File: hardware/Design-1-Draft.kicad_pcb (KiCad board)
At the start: 2 copper layers, 2 parts

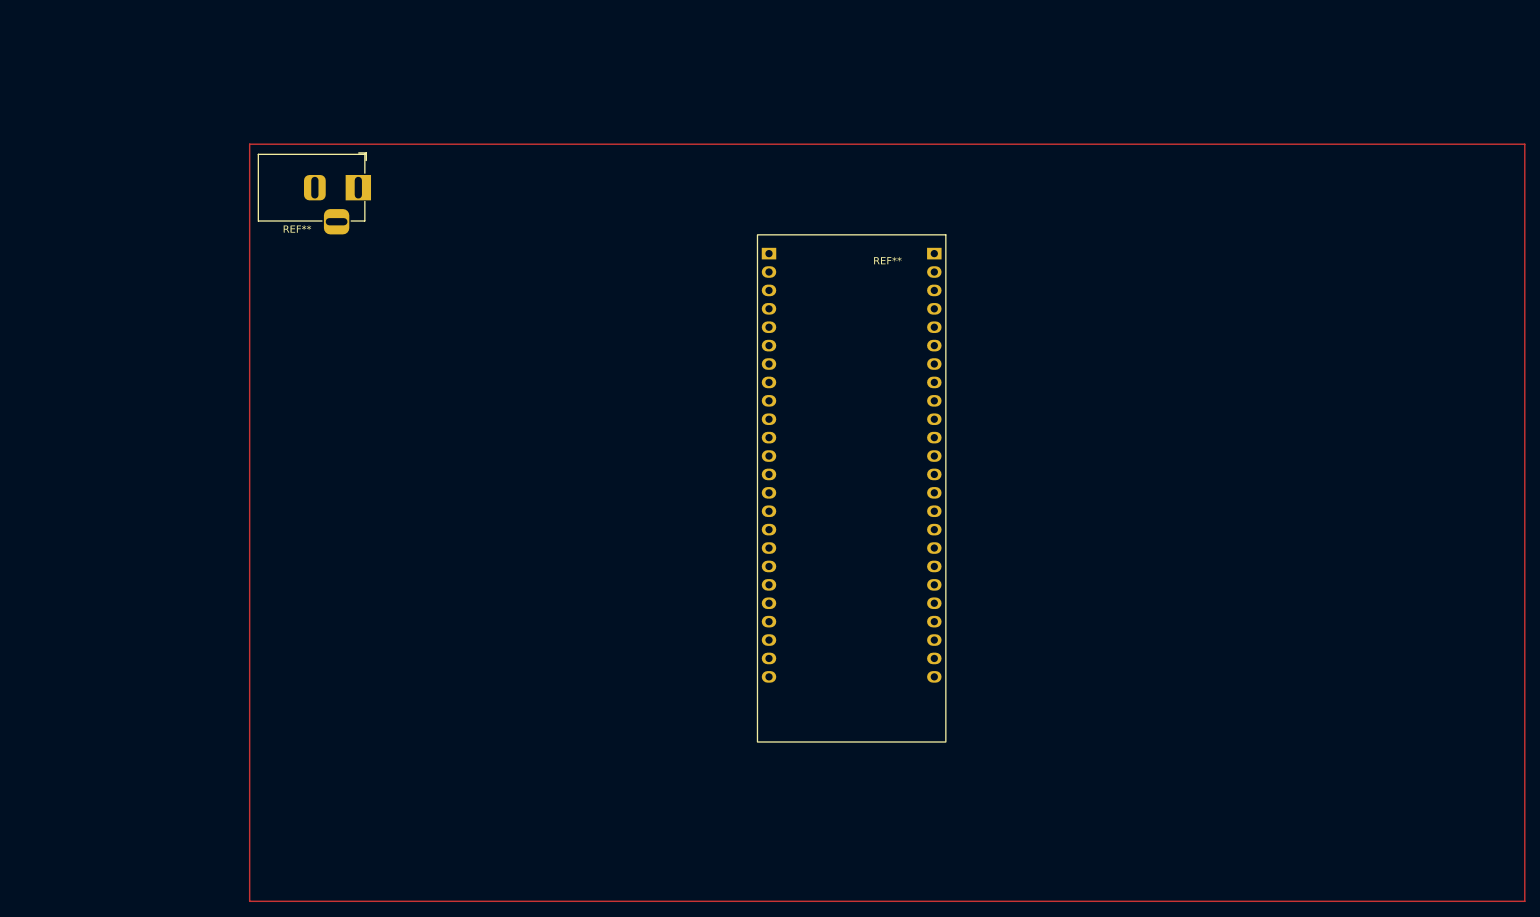
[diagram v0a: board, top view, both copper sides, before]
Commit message: added fuse, schottky, at adc sa pcb
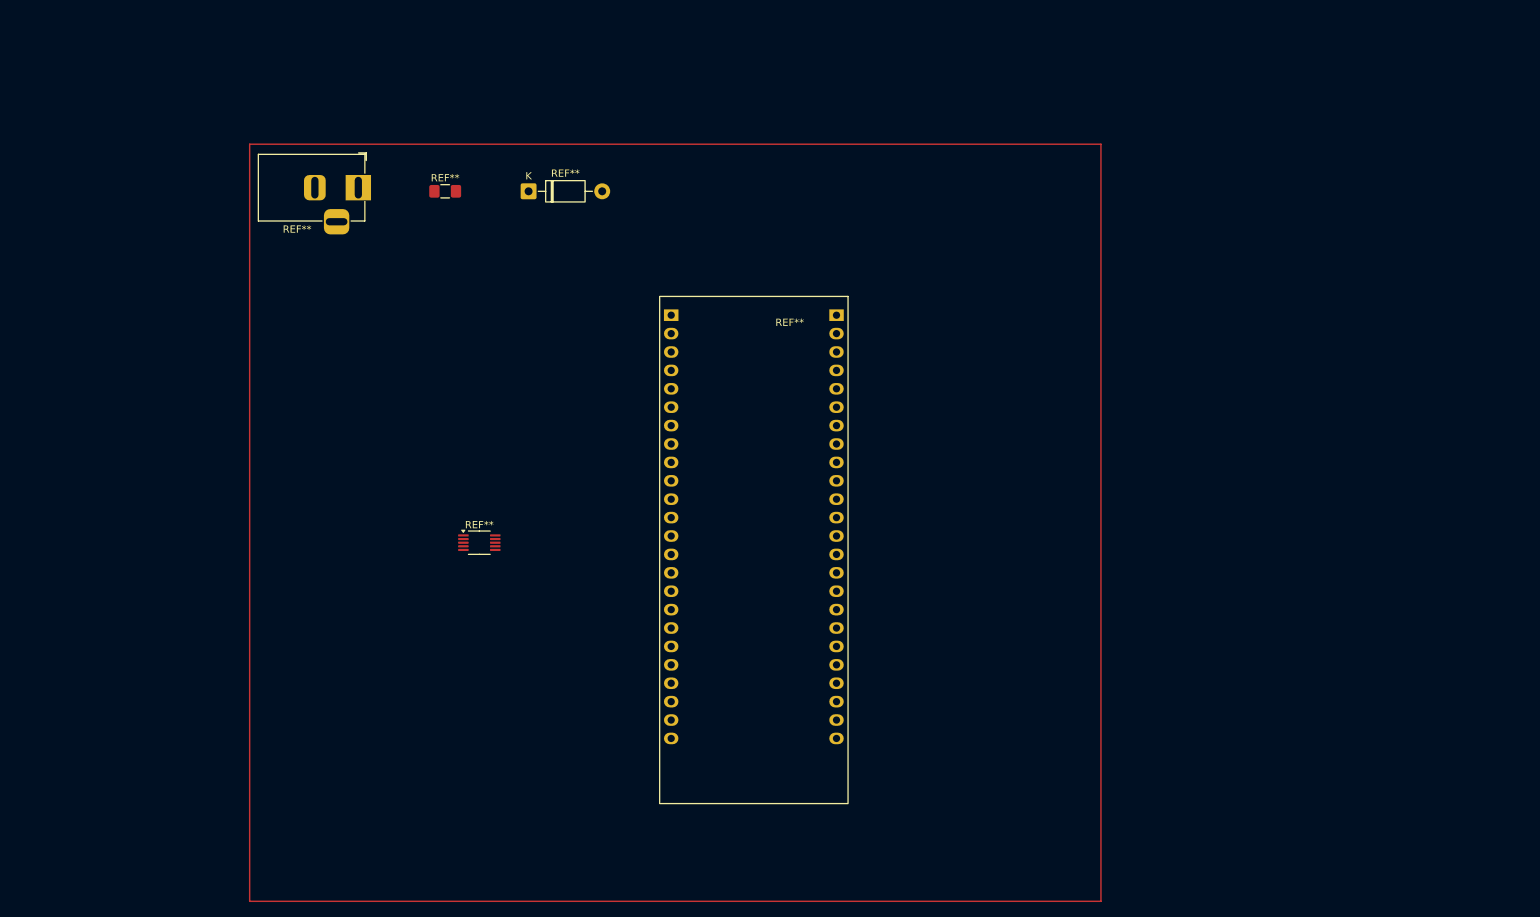
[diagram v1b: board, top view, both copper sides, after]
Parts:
- added REF**: D_DO-41_SOD81_P10.16mm_Horizontal, Diode_THT:D_DO-41_SOD81_P10.16mm_Horizontal, F.Cu at (105.0, 40.5)
- added REF**: VSSOP-10_3x3mm_P0.5mm, Package_SO:VSSOP-10_3x3mm_P0.5mm, F.Cu at (98.2, 89.0)
- added REF**: Fuse_1206_3216Metric_Pad1.42x1.75mm_HandSolder, Fuse:Fuse_1206_3216Metric_Pad1.42x1.75mm_HandSolder, F.Cu at (93.5, 40.5)
- moved REF** 16.0 mm to (136.1, 86.8)

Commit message: Assigned footprints sa schematic (kulang pa ginagawan ko pa yung iba)
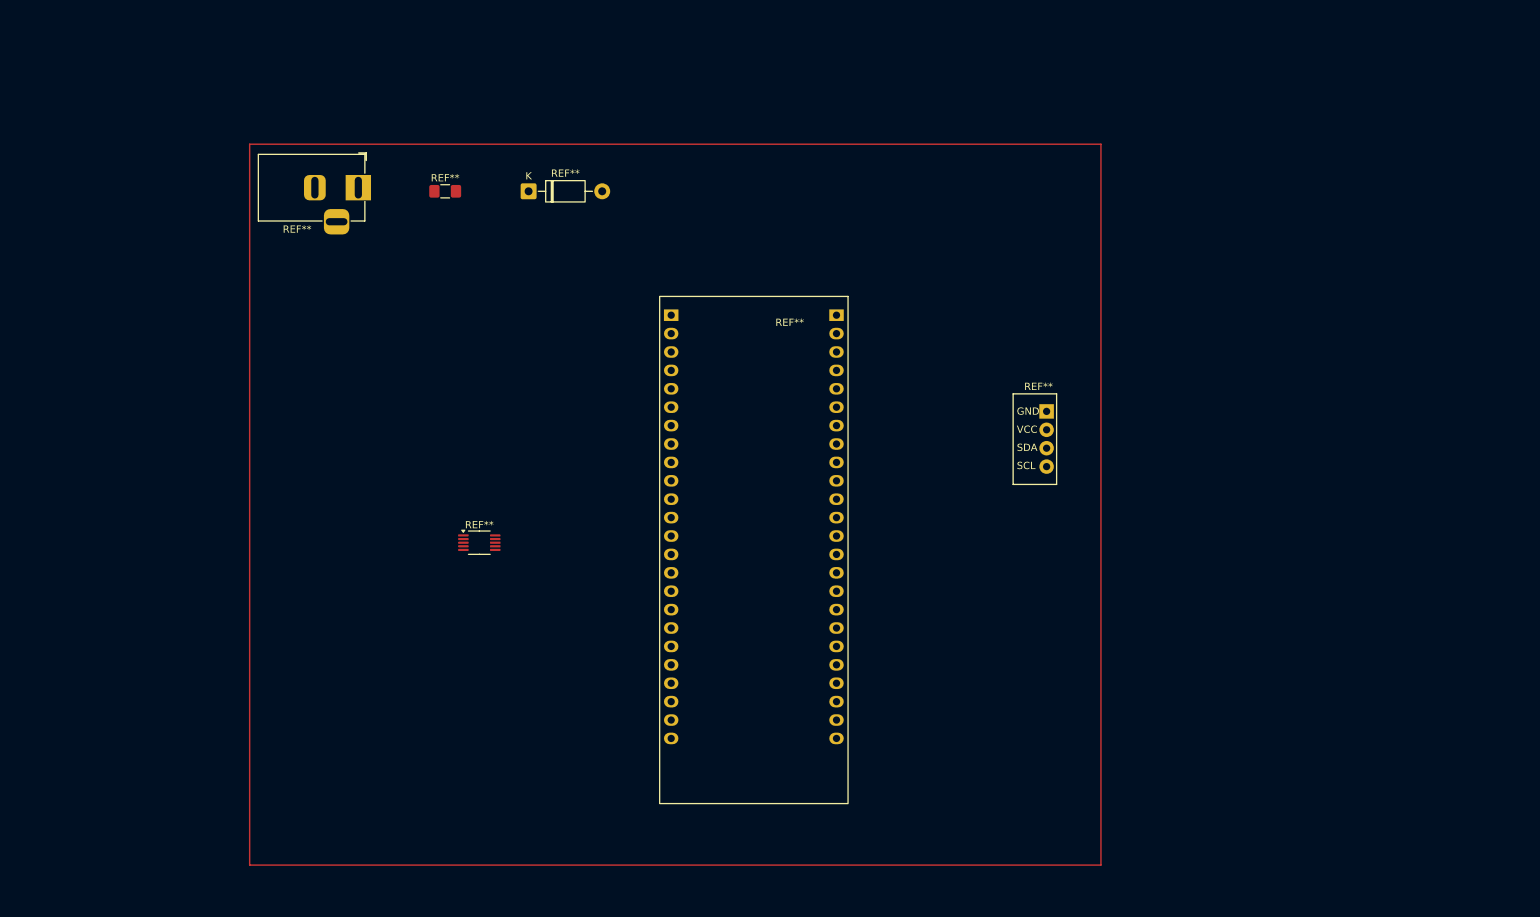
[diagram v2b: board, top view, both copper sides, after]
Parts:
- added REF**: I2C-BACKPACK-LCD, 1_CustomFootprints:I2C-BACKPACK-LCD, F.Cu at (175.0, 74.7)
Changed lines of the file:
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@@
 		)
+	)
+	(footprint "1_CustomFootprints:I2C-BACKPACK-LCD"
+		(layer "F.Cu")
+		(at 175 74.71)
+		(property "Reference" "REF**"
+			(at 0.38 -7.25 0)
+			(unlocked yes)
+			(layer "F.SilkS")
+			(effects
+				(font
+					(size 1 1)
+					(thickness 0.1)
+				)
+			)
+		)
+		(property "Value" "I2C-BACKPACK-LCD"
+			(at 0.38 7.25 0)
+			(unlocked yes)
+			(layer "F.Fab")
+			(effects
+				(font
+					(size 1 1)
+					(thickness 0.15)
+				)
+			)
+		)
+		(property "Datasheet" ""
+			(at 0 0 0)
+			(unlocked yes)
+			(layer "F.Fab")
+			(hide yes)
+			(effects
+				(font
+					(size 1 1)
+					(thickness 0.15)
+				)
+			)
+		)
+		(property "Description" ""
+			(at 0 0 0)
+			(unlocked yes)
+			(layer "F.Fab")
+			(hide yes)
+			(effects
+				(font
+					(size 1 1)
+					(thickness 0.15)
+				)
+			)
+		)
+		(attr smd)
+		(fp_line
+			(start -3.12 -6.25)
+			(end 2.88 -6.25)
+			(stroke
+				(width 0.1)
+				(type default)
+			)
+			(layer "F.SilkS")
+		)
+		(fp_line
+			(start -3.12 6.25)
+			(end -3.12 -6.25)
+			(stroke
+				(width 0.1)
+				(type default)
+			)
+			(layer "F.SilkS")
+		)
+		(fp_line
+			(start 2.88 -6.25)
+			(end 2.88 6.25)
+			(stroke
+				(width 0.1)
+				(type default)
+			)
+			(layer "F.SilkS")
+		)
+		(fp_line
+			(start 2.88 6.25)
+			(end -3.12 6.25)
+			(stroke
+				(width 0.1)
+				(type default)
+			)
+			(layer "F.SilkS")
+		)
+		(fp_text user "VCC"
+			(at -2.62 -0.75 0)
+			(unlocked yes)
+			(layer "F.SilkS")
+			(effects
+				(font
+					(size 1 1)
+					(thickness 0.1)
+				)
+				(justify left bottom)
+			)
+		)
+		(fp_text user "GND"
+			(at -2.62 -3.25 0)
+			(unlocked yes)
+			(layer "F.SilkS")
+			(effects
+				(font
+					(size 1 1)
+					(thickness 0.1)
+				)
+				(justify left bottom)
+			)
+		)
+		(fp_text user "SCL"
+			(at -2.62 4.25 0)
+			(unlocked yes)
+			(layer "F.SilkS")
+			(effects
+				(font
+					(size 1 1)
+					(thickness 0.1)
+				)
+				(justify left bottom)
+			)
+		)
+		(fp_text user "SDA"
+			(at -2.62 1.75 0)
+			(unlocked yes)
+			(layer "F.SilkS")
+			(effects
+				(font
+					(size 1 1)
+					(thickness 0.1)
+				)
+				(justify left bottom)
+			)
+		)
+		(pad "1" thru_hole rect
+			(at 1.5 -3.83)
+			(size 2 2)
+			(drill 1)
+			(layers "*.Cu" "*.Mask")
+			(remove_unused_layers no)
+		)
+		(pad "2" thru_hole circle
+			(at 1.5 -1.29)
+			(size 2 2)
+			(drill 1)
+			(layers "*.Cu" "*.Mask")
+			(remove_unused_layers no)
+		)
+		(pad "3" thru_hole circle
+			(at 1.5 1.25)
+			(size 2 2)
+			(drill 1)
+			(layers "*.Cu" "*.Mask")
+			(remove_unused_layers no)
+		)
+		(pad "4" thru_hole circle
+			(at 1.5 3.79)
+			(size 2 2)
+			(drill 1)
+			(layers "*.Cu" "*.Mask")
+			(remove_unused_layers no)
+		)
+		(zone
+			(net 0)
+			(net_name "")
+			(layer "F.SilkS")
+			(hatch edge 0.5)
+			(connect_pads
+				(clearance 0)
+			)
+			(min_thickness 0.25)
+			(filled_areas_thickness no)
+			(keepout
+				(tracks allowed)
+				(vias allowed)
+				(pads not_allowed)
+				(copperpour allowed)
+				(footprints not_allowed)
+			)
+			(placement
+				(enabled no)
+				(sheetname "")
+			)
+			(fill
+				(thermal_gap 0.5)
+				(thermal_bridge_width 0.5)
+			)
+			(polygon
+				(pts
+					(xy 171.88 68.46) (xy 177.88 68.46) (xy 177.88 80.96) (xy 171.88 80.96)
+				)
+			)
+		)
+		(embedded_fonts no)
 	)
 	(footprint "Package_SO:VSSOP-10_3x3mm_P0.5mm"
@@
 	(gr_rect
 		(start 66.5 34)
-		(end 184 138.5)
+		(end 184 133.5)
 		(stroke
 			(width 0.2)

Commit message: added footprints to pcb (not yet complete)
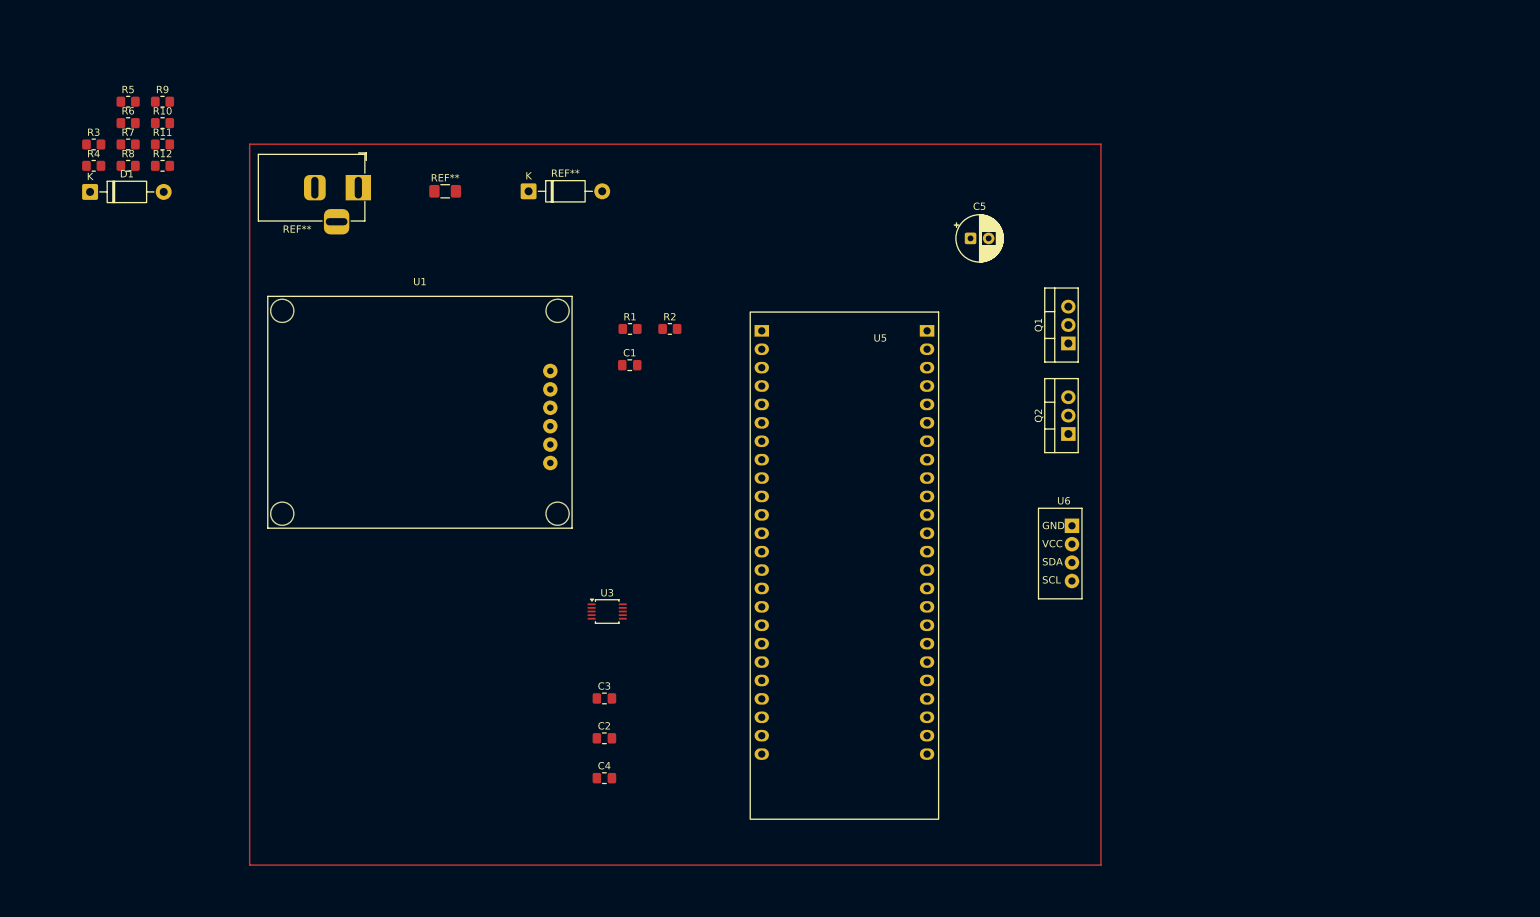
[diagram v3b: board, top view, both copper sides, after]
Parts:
- removed the REF** at (175.0, 74.7)
- removed the REF** at (98.2, 89.0)
- removed the REF** at (136.1, 86.8)
- added C1: 0.1u, Capacitor_SMD:C_0805_2012Metric_Pad1.18x1.45mm_HandSolder, F.Cu at (119.0, 64.5)
- added C2: 0.1u, Capacitor_SMD:C_0805_2012Metric_Pad1.18x1.45mm_HandSolder, F.Cu at (115.5, 116.0)
- added C3: 0.1u, Capacitor_SMD:C_0805_2012Metric_Pad1.18x1.45mm_HandSolder, F.Cu at (115.5, 110.5)
- added C4: 10u, Capacitor_SMD:C_0805_2012Metric_Pad1.18x1.45mm_HandSolder, F.Cu at (115.5, 121.5)
- added C5: 470u, Capacitor_THT:CP_Radial_D6.3mm_P2.50mm, F.Cu at (166.0, 47.0)
- added D1: D_Schottky, Diode_THT:D_DO-41_SOD81_P10.16mm_Horizontal, F.Cu at (44.5, 40.6)
- added Q1: IRLZ44N, Package_TO_SOT_THT:TO-220-3_Vertical, F.Cu at (179.5, 61.5)
- added Q2: IRLZ44N, Package_TO_SOT_THT:TO-220-3_Vertical, F.Cu at (179.5, 74.0)
- added R1: 22k, Resistor_SMD:R_0805_2012Metric_Pad1.20x1.40mm_HandSolder, F.Cu at (119.0, 59.5)
- added R10: 10k, Resistor_SMD:R_0805_2012Metric_Pad1.20x1.40mm_HandSolder, F.Cu at (54.5, 31.1)
- added R11: 100, Resistor_SMD:R_0805_2012Metric_Pad1.20x1.40mm_HandSolder, F.Cu at (54.5, 34.0)
- added R12: 10k, Resistor_SMD:R_0805_2012Metric_Pad1.20x1.40mm_HandSolder, F.Cu at (54.5, 37.0)
- added R2: 12k, Resistor_SMD:R_0805_2012Metric_Pad1.20x1.40mm_HandSolder, F.Cu at (124.5, 59.5)
- added R3: 1k, Resistor_SMD:R_0805_2012Metric_Pad1.20x1.40mm_HandSolder, F.Cu at (45.0, 34.0)
- added R4: 4.7k, Resistor_SMD:R_0805_2012Metric_Pad1.20x1.40mm_HandSolder, F.Cu at (45.0, 37.0)
- added R5: 4.7k, Resistor_SMD:R_0805_2012Metric_Pad1.20x1.40mm_HandSolder, F.Cu at (49.7, 28.1)
- added R6: 4.7k, Resistor_SMD:R_0805_2012Metric_Pad1.20x1.40mm_HandSolder, F.Cu at (49.7, 31.1)
- added R7: 100, Resistor_SMD:R_0805_2012Metric_Pad1.20x1.40mm_HandSolder, F.Cu at (49.7, 34.0)
- added R8: 10k, Resistor_SMD:R_0805_2012Metric_Pad1.20x1.40mm_HandSolder, F.Cu at (49.7, 37.0)
- added R9: 100, Resistor_SMD:R_0805_2012Metric_Pad1.20x1.40mm_HandSolder, F.Cu at (54.5, 28.1)
- added U1: ~, 1_CustomFootprints:PH-4502C, F.Cu at (90.0, 71.0)
- added U3: ADS1115IDGS, Package_SO:TSSOP-10_3x3mm_P0.5mm, F.Cu at (115.8, 98.5)
- added U5: Tang_Nano_9K, 0my_project:DIP-48_TangNano9K, F.Cu at (148.6, 89.0)
- added U6: ~, 1_CustomFootprints:I2C-BACKPACK-LCD, F.Cu at (178.5, 90.5)

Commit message: updated footprint lib
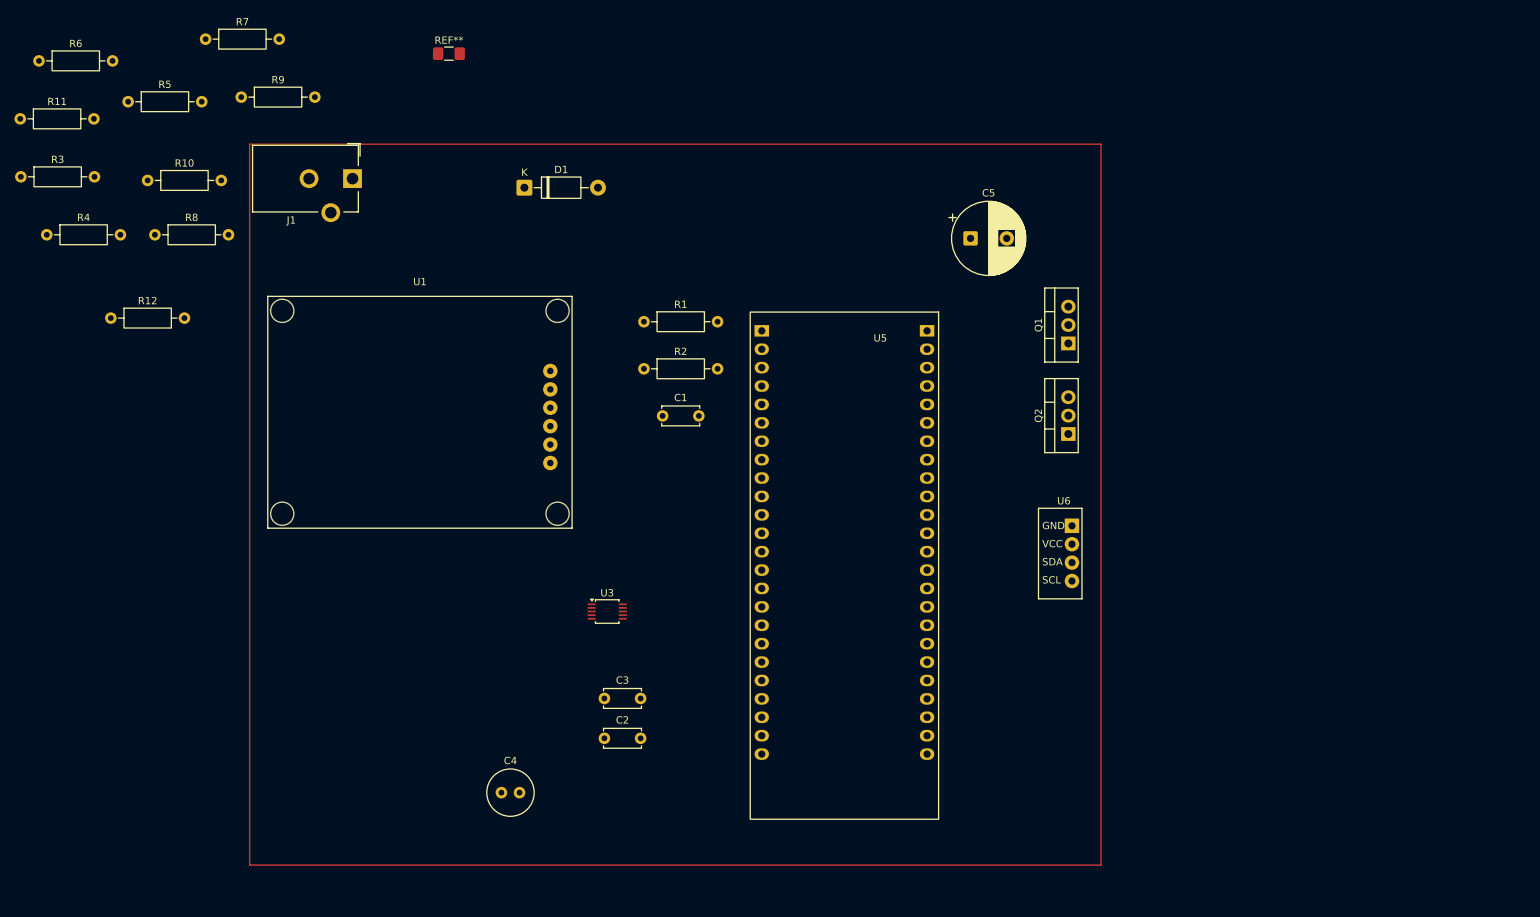
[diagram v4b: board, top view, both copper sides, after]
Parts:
- removed the REF** at (105.0, 40.5)
- removed the REF** at (81.5, 40.0)
- added J1: Barrel_Jack_Switch, Connector_BarrelJack:BarrelJack_CUI_PJ-102AH_Horizontal, F.Cu at (80.7, 38.8)
- C1, C2, C3: footprint Capacitor_SMD:C_0805_2012Metric_Pad1.18x1.45mm_HandSolder -> Capacitor_THT:C_Disc_D5.0mm_W2.5mm_P5.00mm
- C4: footprint Capacitor_SMD:C_0805_2012Metric_Pad1.18x1.45mm_HandSolder -> Capacitor_THT:C_Radial_D6.3mm_H5.0mm_P2.50mm
- C5: footprint Capacitor_THT:CP_Radial_D6.3mm_P2.50mm -> Capacitor_THT:CP_Radial_D10.0mm_P5.00mm
- R1, R10, R11, R12, R2, R3, R4, R5, R6, R7, R8, R9: footprint Resistor_SMD:R_0805_2012Metric_Pad1.20x1.40mm_HandSolder -> Resistor_THT:R_Axial_DIN0207_L6.3mm_D2.5mm_P10.16mm_Horizontal
- moved D1 59.9 mm to (104.4, 40.0)
- moved R12 22.2 mm to (47.3, 58.0)
- moved R11 20.0 mm to (34.8, 30.5)
- moved REF** 19.0 mm to (94.0, 21.5)
- moved R7 18.0 mm to (60.4, 19.5)
- moved R6 15.0 mm to (37.4, 22.5)
- moved C4 14.4 mm to (101.2, 123.5)
- moved R4 11.5 mm to (38.5, 46.5)
- moved R3 11.0 mm to (34.9, 38.5)
- moved R9 10.9 mm to (65.3, 27.5)
- moved R8 10.2 mm to (53.4, 46.5)
- moved C1 8.34 mm to (123.5, 71.5)
- moved R10 8.18 mm to (52.4, 39.0)
- moved R2 6.56 mm to (120.9, 65.0)
- moved R1 2.16 mm to (120.9, 58.5)
